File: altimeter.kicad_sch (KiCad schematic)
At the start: 40 parts, among them J1 USB_C_Receptacle_USB2.0_16P, J3 TagConnect, SW2 SW_SPDT, U1 nRF52833_QDxx, U2 MCP73832, U3 BMP390L, U4 W25X40CLUXIG, U5 LIS2DH, Y1 Crystal_GND24

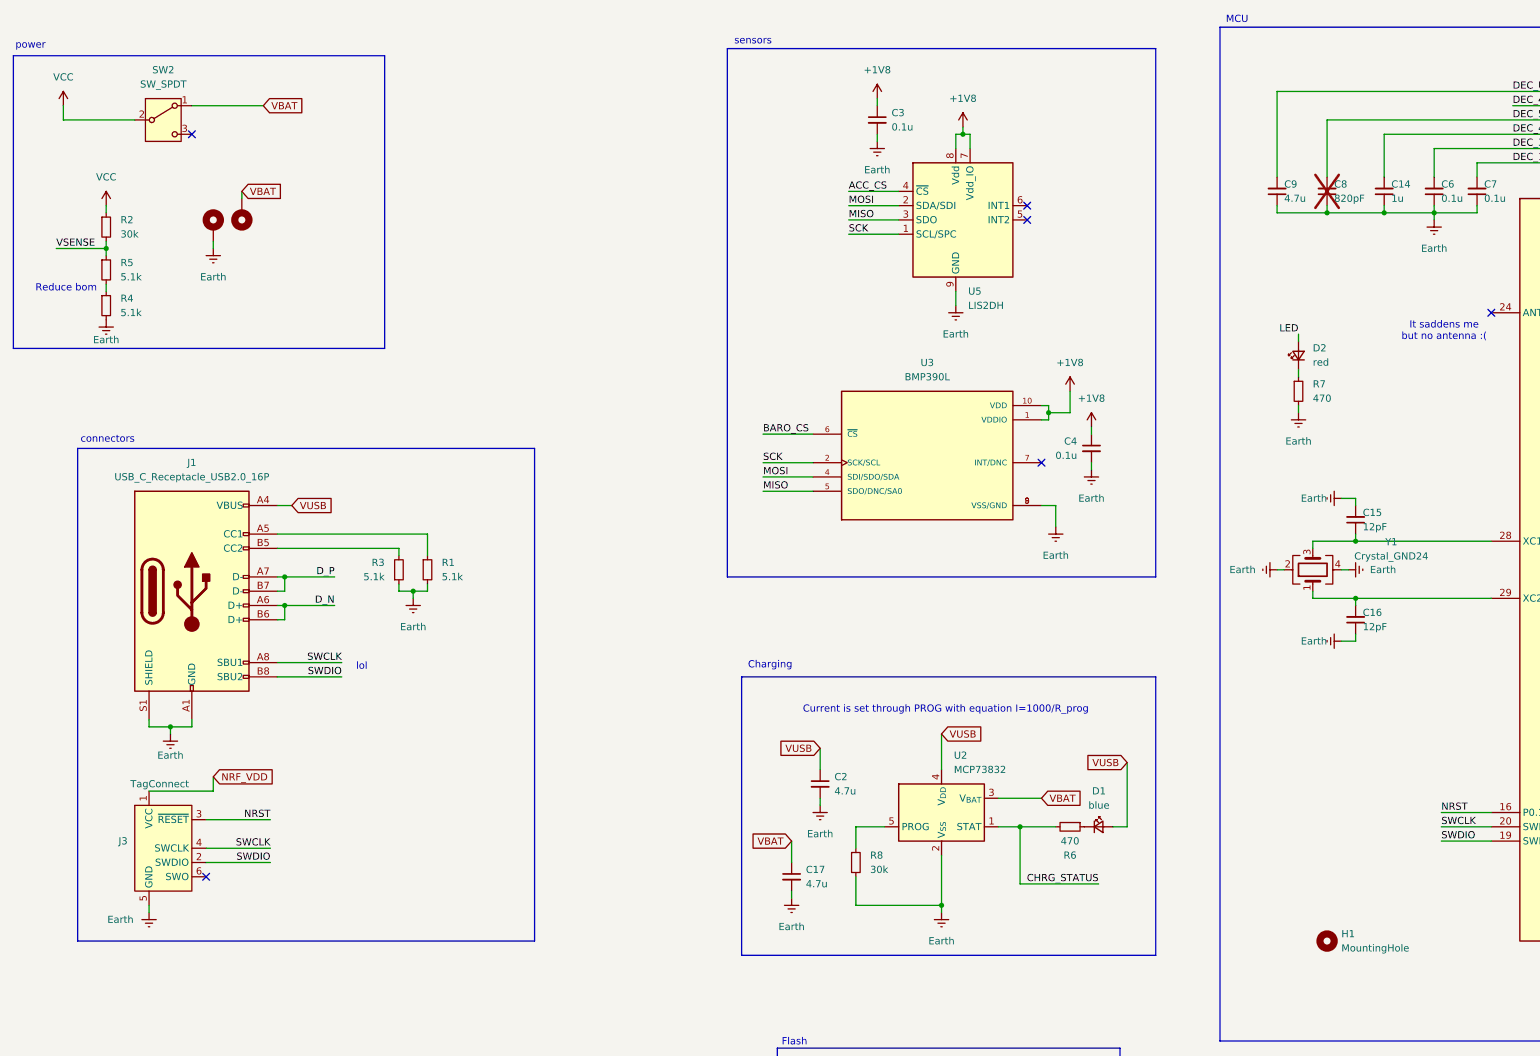
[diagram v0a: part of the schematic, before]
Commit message: add LCSC BOM
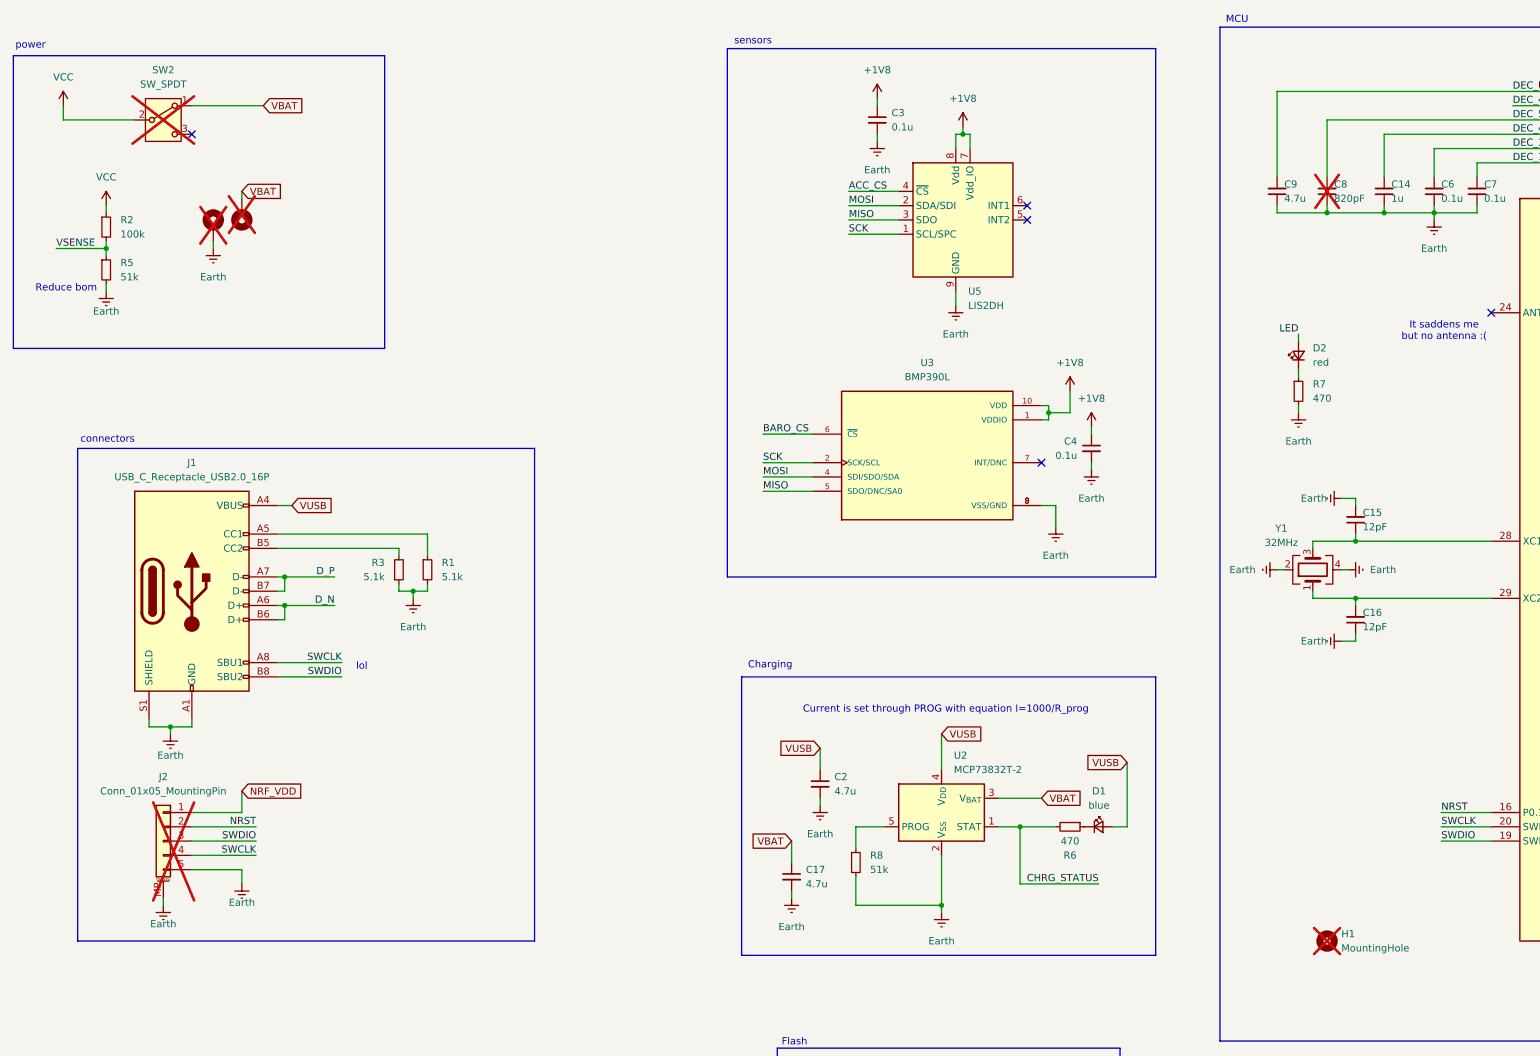
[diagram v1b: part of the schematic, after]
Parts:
- removed J3: TagConnect, Connector:Tag-Connect_TC2030-IDC-NL_2x03_P1.27mm_Vertical, symbol Connector:Conn_ARM_SWD_TagConnect_TC2030-NL
- removed R4: 5.1k, Resistor_SMD:R_0402_1005Metric, symbol Device:R_Small
- added J2: Conn_01x05_MountingPin, Connector_JST:JST_SH_BM05B-SRSS-TB_1x05-1MP_P1.00mm_Vertical, symbol Connector_Generic_MountingPin:Conn_01x05_MountingPin
- C1, C11, C18, C3, C4, C5, C6, C7: LCSC (none) -> C1525
- C10, C12, C13, C17, C2, C9: LCSC (none) -> C23733
- C14: LCSC (none) -> C52923
- D1: LCSC (none) -> C131223
- D2: LCSC (none) -> C7420553
- H1, H2, H3, SW2: now not fitted
- J1: LCSC (none) -> C2765186
- R1, R3: LCSC (none) -> C25905
- R2: value 30k -> 100k; LCSC (none) -> C25741
- R5: value 5.1k -> 51k; LCSC (none) -> C25794
- R6, R7: LCSC (none) -> C25117
- R8: value 30k -> 51k; LCSC (none) -> C25794
- U1: LCSC (none) -> C2895249
- U2: value MCP73832 -> MCP73832T-2; LCSC (none) -> C38066
- U3: LCSC (none) -> C779278
- U4: LCSC (none) -> C401661
- U5: LCSC (none) -> C155670
- Y1: value Crystal_GND24 -> 32MHz; LCSC (none) -> C5830663
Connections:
- net Earth: now also R5.2, J2.5 (Pin_5), J2.MP (MountPin)
- net NRF_VDD: now also J2.1 (Pin_1)
- net NRST: now also J2.2 (Pin_2)
- net SWCLK: now also J2.4 (Pin_4)
- net SWDIO: now also J2.3 (Pin_3)
- no-connect marks 13 -> 12

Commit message: ordered version
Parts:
- C15, C16: value 12pF -> 12p
- C6: value 0.1u -> 100p; LCSC C1525 -> C1546
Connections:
- net D_N: now also J1.A7 (D-), J1.B7 (D-); no longer J1.A6 (D+), J1.B6 (D+)
- net D_P: now also J1.A6 (D+), J1.B6 (D+); no longer J1.A7 (D-), J1.B7 (D-)
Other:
- moved on the sheet: C18, U4
